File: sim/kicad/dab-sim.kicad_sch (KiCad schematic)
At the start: 25 parts

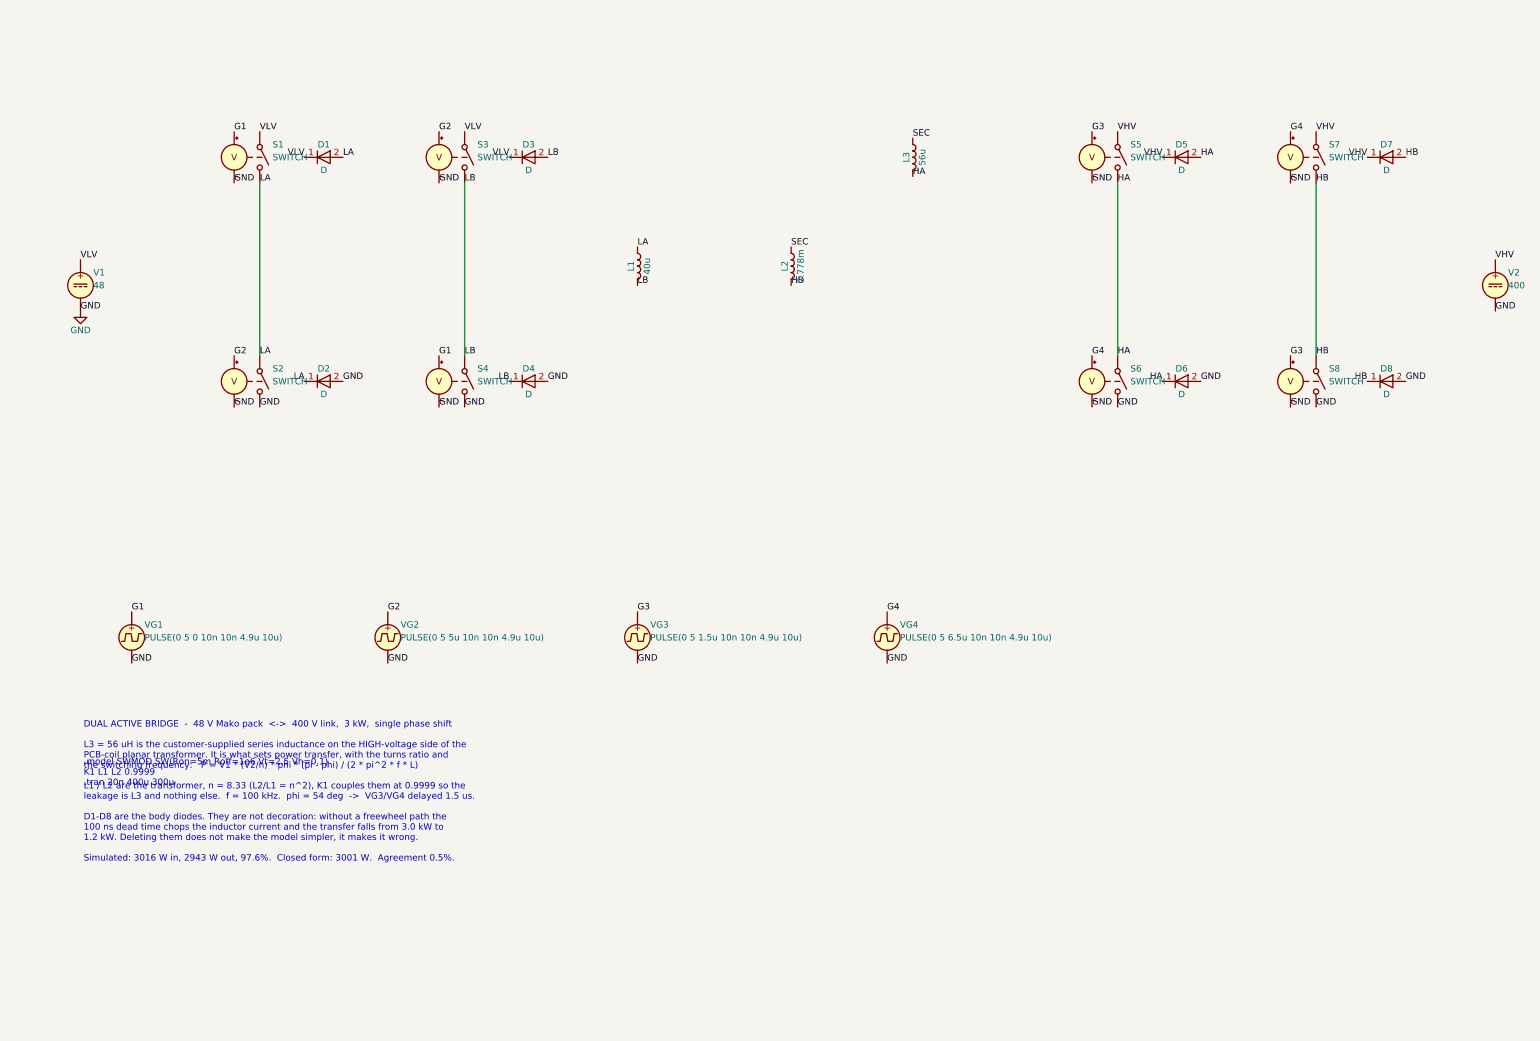
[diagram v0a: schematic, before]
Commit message: Redraw the DAB schematic with wires instead of net labels
A schematic wired only by net names is correct for the netlister and
useless to a human - you cannot trace the bridge by eye. Rebuilt so that
every power connection is a drawn line: both DC rails, the four bridge
legs, the body diodes, the transformer between the low-voltage midpoints
and the 56 uH in the secondary path. Only the four gate nets stay as
labels, which is normal practice; drawing them would put eight wires
across the sheet for nothing. The power nets now carry names as well as
wires, so the exported netlist reads VLV_48V / LA / LB / HA / HB /
VHV_400V rather than Net-_D1-A_.

The rails are drawn above and below the switch rows with stubs down to
each pin, not straight across them: the SWITCH symbol puts its control
pins at the same heights as its power pins, so a rail across a switch row
shorts the supply to the gate net. That is in the README, along with the
Sim.* instance-property trap.

Rebuilt from scratch and independently reproduces the previous result:
3005 W in, 2938 W out, 97.8%, against the closed form's 3001 W - 0.1%.

Co-Authored-By: Claude Opus 5 <noreply@anthropic.com>
Claude-Session: https://claude.ai/code/session_018xNdiSQv3JdagdWVUHe6u6
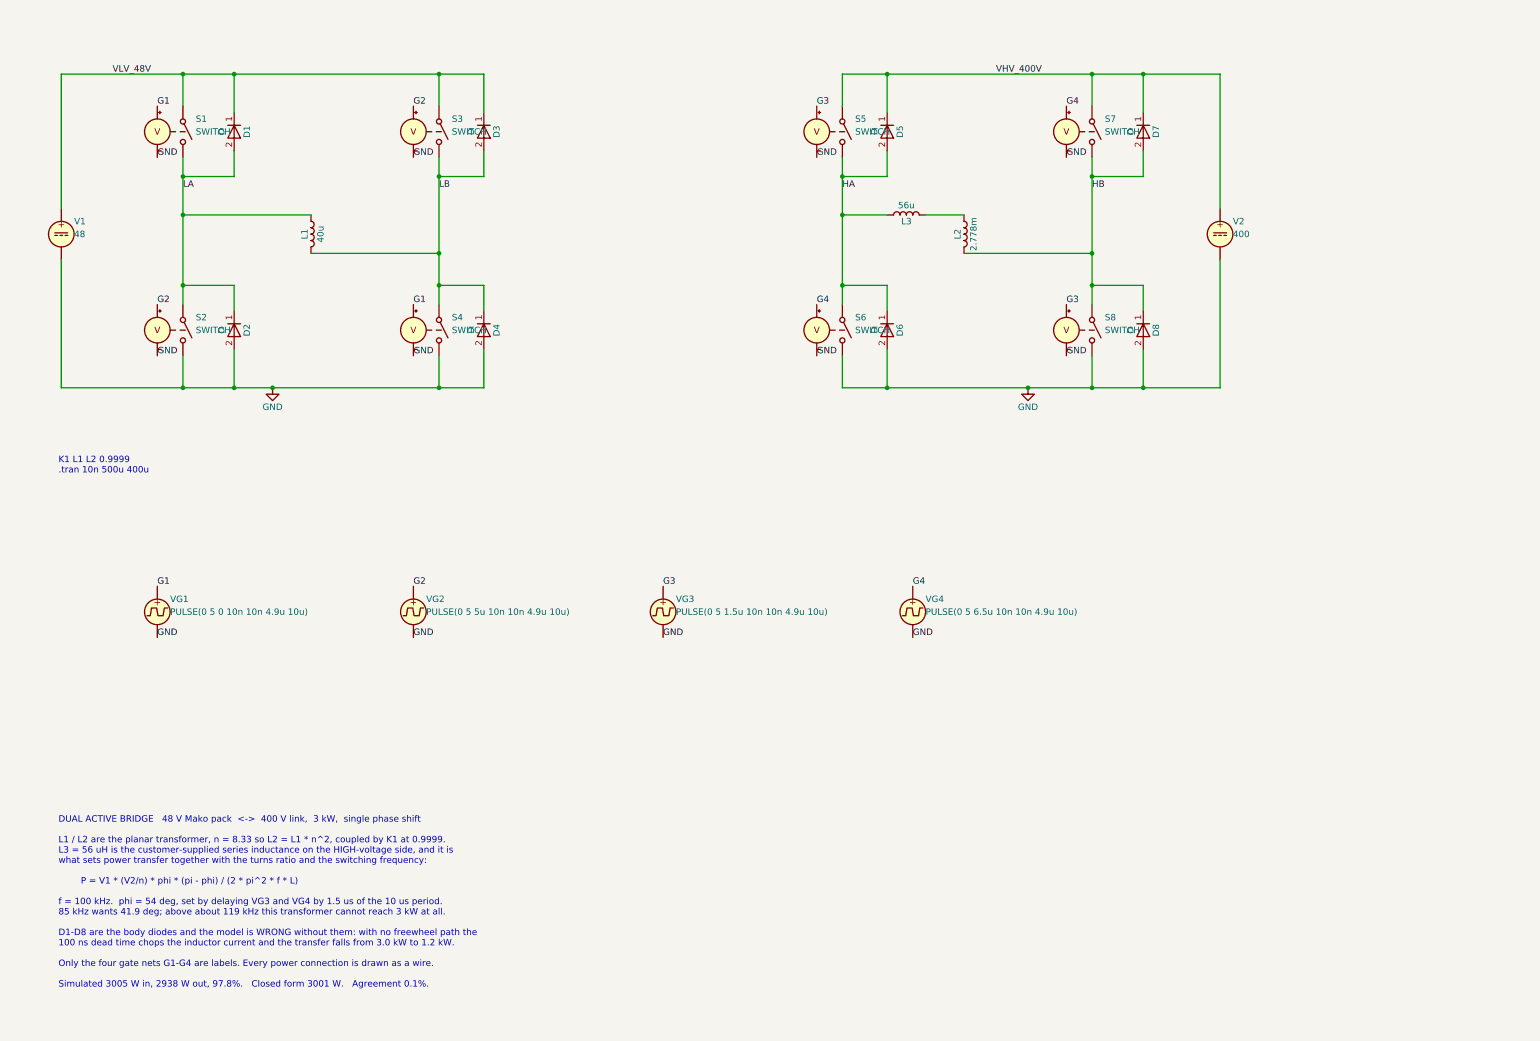
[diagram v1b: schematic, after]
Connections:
- net HA: now also L3.1; no longer L3.2
- net SEC: no longer names the net of L2.1
- net SEC: now also L3.2; no longer L3.1
- net VHV renamed VHV_400V
- net VLV renamed VLV_48V
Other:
- note added: "DUAL ACTIVE BRIDGE 48 V Mako pack <-> 400 V link, 3 kW, single phase shift L1 / L2 are the planar transformer, n = 8.33 so L2 = L1 * n^2, coupled by K1 at 0.9999. L3 = 56 uH is the customer-supplied series inductance on the HIGH-voltage side, and it is what sets power transfer together with the turns ratio and the switching frequency: P = V1 * (V2/n) * phi * (pi - phi) / (2 * pi^2 * f * L) f = 10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"
- note added: "K1 L1 L2 0.9999 .tran 10n 500u 400u"
- note removed: ".model SWMOD SW(Ron=5m Roff=1e6 Vt=2.5 Vh=0.1) K1 L1 L2 0.9999 .tran 20n 400u 300u"
- note removed: "DUAL ACTIVE BRIDGE - 48 V Mako pack <-> 400 V link, 3 kW, single phase shift L3 = 56 uH is the customer-supplied series inductance on the HIGH-voltage side of the PCB-coil planar transformer. It is what sets power transfer, with the turns ratio and the switching frequency: P = V1 * (V2/n) * phi * (pi - phi) / (2 * pi^2 * f * L) L1 / L2 are the transformer, n = 8.33 (L2/L1 = n^2), K1 couples them 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"

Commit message: Replace the K directive with a transformer subcircuit KiCad resolves itself
Three failures in a row all had the same root: mutual coupling reaching
ngspice through schematic text. K is a DEVICE line, not a dot command, and
the GUI netlister prepends a dot to any directive lacking one, so a bare K
arrives as ".k1" and the circuit will not parse. A relative .include fails
too - KiCad drives ngspice as a shared library and hands it the netlist in
memory, leaving no file for a relative path to resolve against.

The windings and their coupling now live in xfmr.lib as a subcircuit,
attached to a real Device:Transformer_1P_1S symbol by Sim.Library =
${KIPRJMOD}/xfmr.lib. Verified that KiCad resolves that variable itself
and emits an absolute, quoted .include: absolute so the shared library
finds it, quoted so a path containing spaces works, and portable because
the variable is resolved at netlist time. Verified separately that
${KIPRJMOD} is NOT expanded in schematic text, which is why the directive
route could never have been made portable.

The sheet also reads better for it: two H-bridges either side of an actual
transformer symbol, with the 56 uH in the secondary, rather than two
disconnected inductors coupled by an invisible statement.

Caught and fixed a short of my own making on the way - the wire routing
pin AA around to the far bridge leg ran straight through pin AB, which the
netlist showed as "XT1 /LA /LA". Also removed four floating wire stubs
left where L1 and L2 had been.

Electrically identical to the verified version, to six figures: 3005.3 W
in, 2938.4 W out, 9.511 A rms, against the closed form's 3001 W.

Co-Authored-By: Claude Opus 5 <noreply@anthropic.com>
Claude-Session: https://claude.ai/code/session_018xNdiSQv3JdagdWVUHe6u6
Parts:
- removed L1: 40u, symbol Device:L
- removed L2: 2.778m, symbol Device:L
- added T1: XFMR 8.33:1, symbol Device:Transformer_1P_1S
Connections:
- net HA: now also L3.2; no longer L3.1
- net HB: now also T1.4 (SB)
- net LA: now also T1.1 (AA)
- net LB: now also T1.2 (AB)
- new net: L3.1, T1.3 (SA)
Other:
- note added: ".tran 10n 500u 400u"
- note added: "DUAL ACTIVE BRIDGE 48 V Mako pack <-> 400 V link, 3 kW, single phase shift T1 is the planar transformer, n = 8.33. Its windings and their mutual coupling live in xfmr.lib, attached to T1 by Sim.Library = ${KIPRJMOD}/xfmr.lib, and KiCad resolves that itself into an absolute .include when it builds the netlist. That indirection is not decoration. K is a DEVICE line in SPICE, not a dot command, and 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"
- note removed: "DUAL ACTIVE BRIDGE 48 V Mako pack <-> 400 V link, 3 kW, single phase shift L1 / L2 are the planar transformer, n = 8.33 so L2 = L1 * n^2, coupled by K1 at 0.9999. L3 = 56 uH is the customer-supplied series inductance on the HIGH-voltage side, and it is what sets power transfer together with the turns ratio and the switching frequency: P = V1 * (V2/n) * phi * (pi - phi) / (2 * pi^2 * f * L) f = 10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"
- note removed: "K1 L1 L2 0.9999 .tran 10n 500u 400u"
- moved on the sheet: L3
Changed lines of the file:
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@@
-	)
-	(junction
-		(at 59.69 96.52)
-		(diameter 0)
-	)
-	(junction
-		(at 110.49 104.14)
-		(diameter 0)
 	)
 	(junction
@@
 	)
 	(junction
-		(at 190.5 96.52)
-		(diameter 0)
-	)
-	(junction
-		(at 240.03 104.14)
-		(diameter 0)
-	)
-	(junction
 		(at 77.47 130.81)
 		(diameter 0)
@@
 		(diameter 0)
 	)
+	(junction
+		(at 110.49 105.41)
+		(diameter 0)
+	)
+	(junction
+		(at 139.7 105.41)
+		(diameter 0)
+	)
+	(junction
+		(at 59.69 100.33)
+		(diameter 0)
+	)
+	(junction
+		(at 190.5 105.41)
+		(diameter 0)
+	)
+	(junction
+		(at 240.03 100.33)
+		(diameter 0)
+	)
 	(wire
 		(pts
@@
 	(wire
 		(pts
-			(xy 59.69 96.52)
-			(xy 85.09 96.52)
-		)
-	)
-	(wire
-		(pts
-			(xy 85.09 104.14)
-			(xy 110.49 104.14)
-		)
-	)
-	(wire
-		(pts
 			(xy 265.43 95.25)
 			(xy 265.43 68.58)
@@
 	(wire
 		(pts
-			(xy 190.5 96.52)
-			(xy 199.39 96.52)
-		)
-	)
-	(wire
-		(pts
-			(xy 207.01 96.52)
-			(xy 214.63 96.52)
-		)
-	)
-	(wire
-		(pts
-			(xy 214.63 104.14)
-			(xy 240.03 104.14)
-		)
-	)
-	(text "K1 L1 L2 0.9999\n.tran 10n 500u 400u"
-		(at 35 148 0)
+			(xy 139.7 105.41)
+			(xy 110.49 105.41)
+		)
+	)
+	(wire
+		(pts
+			(xy 25.4 100.33)
+			(xy 59.69 100.33)
+		)
+	)
+	(wire
+		(pts
+			(xy 160.02 105.41)
+			(xy 171.45 105.41)
+		)
+	)
+	(wire
+		(pts
+			(xy 179.07 105.41)
+			(xy 190.5 105.41)
+		)
+	)
+	(wire
+		(pts
+			(xy 160.02 95.25)
+			(xy 160.02 59.69)
+		)
+	)
+	(wire
+		(pts
+			(xy 160.02 59.69)
+			(xy 275.59 59.69)
+		)
+	)
+	(wire
+		(pts
+			(xy 275.59 59.69)
+			(xy 275.59 100.33)
+		)
+	)
+	(wire
+		(pts
+			(xy 275.59 100.33)
+			(xy 240.03 100.33)
+		)
+	)
+	(wire
+		(pts
+			(xy 139.7 95.25)
+			(xy 139.7 55.88)
+		)
+	)
+	(wire
+		(pts
+			(xy 139.7 55.88)
+			(xy 25.4 55.88)
+		)
+	)
+	(wire
+		(pts
+			(xy 25.4 55.88)
+			(xy 25.4 100.33)
+		)
+	)
+	(text ".tran 10n 500u 400u"
+		(at 35 160 0)
 		(effects
 			(font
@@
 		)
 	)
-  (text "DUAL ACTIVE BRIDGE   48 V Mako pack  <->  400 V link,  3 kW,  single phase shift\n\nL1 / L2 are the planar transformer, n = 8.33 so L2 = L1 * n^2, coupled by K1 at 0.9999.\nL3 = 56 uH is the customer-supplied series inductance on the HIGH-voltage side, and it is\nwhat sets power transfer together with the turns ratio and the switching frequency:\n\n        P = V1 * (V2/n) * phi * (pi - phi) / (2 * pi^2 * f * L)\n\nf = 100 kHz.  phi = 54 deg, set by delaying VG3 and VG4 by 1.5 us of the 10 us period.\n85 kHz wants 41.9 deg; above about 119 kHz this transformer cannot reach 3 kW at all.\n\nD1-D8 are the body diodes and the model is WRONG without them: with no freewheel path the\n100 ns dead time chops the inductor current and the transfer falls from 3.0 kW to 1.2 kW.\n\nOnly the four gate nets G1-G4 are labels. Every power connection is drawn as a wire.\n\nSimulated 3005 W in, 2938 W out, 97.8%.   Closed form 3001 W.   Agreement 0.1%."
-    (at 35 250 0)
+  (text "DUAL ACTIVE BRIDGE   48 V Mako pack  <->  400 V link,  3 kW,  single phase shift\n\nT1 is the planar transformer, n = 8.33. Its windings and their mutual coupling live in\nxfmr.lib, attached to T1 by Sim.Library = ${KIPRJMOD}/xfmr.lib, and KiCad resolves that\nitself into an absolute .include when it builds the netlist.\n\nThat indirection is not decoration. K is a DEVICE line in SPICE, not a dot command, and\nthe GUI simulator prepends a dot to any schematic text directive that lacks one - so a\nbare \"K1 L1 L2 0.9999\" on the sheet reaches ngspice as \".k1 ...\" and the circuit will not\nparse. A relative \".include\" does not work either, because KiCad drives ngspice as a\nshared library and hands it the netlist in memory, with no file for a relative path to\nresolve against. Sim.Library avoids both: KiCad does the resolving.\n\nL3 = 56 uH is the customer-supplied series inductance on the HIGH-voltage side, and with\nthe turns ratio and the frequency it is what sets power transfer:\n\n        P = V1 * (V2/n) * phi * (pi - phi) / (2 * pi^2 * f * L)\n\nf = 100 kHz.  phi = 54 deg, set by delaying VG3 and VG4 by 1.5 us of the 10 us period.\n85 kHz wants 41.9 deg; above about 119 kHz this transformer cannot reach 3 kW at all.\n\nD1-D8 are the body diodes and the model is WRONG without them: with no freewheel path the\n100 ns dead time chops the inductor current and the transfer falls from 3.0 kW to 1.2 kW.\n\nOnly the four gate nets G1-G4 are labels. Every power connection is drawn as a wire.\n\nSimulated 3005 W in, 2938 W out, 97.8%.   Closed form 3001 W.   Agreement 0.1%."
+    (at 35 255 0)
     (effects (font (size 1.27 1.27)) (justify left bottom))
   )
@@
 	(symbol
 		(lib_id "Device:L")
-		(at 85.09 100.33 0)
-		(unit 1)
-		(in_bom yes)
-		(on_board yes)
-		(dnp no)
-		(property "Reference" "L1"
-			(at 83.82 100.33 90)
-			(effects
-				(font
-					(size 1.27 1.27)
-				)
-			)
-		)
-		(property "Value" "40u"
-			(at 86.995 100.33 90)
-			(effects
-				(font
-					(size 1.27 1.27)
-				)
-			)
-		)
-		(property "Footprint" ""
-			(at 85.09 100.33 0)
-			(hide yes)
-			(effects
-				(font
-					(size 1.27 1.27)
-				)
-			)
-		)
-		(property "Datasheet" ""
-			(at 85.09 100.33 0)
-			(hide yes)
-			(effects
-				(font
-					(size 1.27 1.27)
-				)
-			)
-		)
-		(instances
-			(project "dab-sim"
-				(path "8bdc63a0-d120-4e49-a0a7-406cc55b9f90"
-					(reference "L1")
-					(unit 1)
-				)
-			)
-		)
-	)
-	(symbol
-		(lib_id "Device:L")
-		(at 214.63 100.33 0)
-		(unit 1)
-		(in_bom yes)
-		(on_board yes)
-		(dnp no)
-		(property "Reference" "L2"
-			(at 213.36 100.33 90)
-			(effects
-				(font
-					(size 1.27 1.27)
-				)
-			)
-		)
-		(property "Value" "2.778m"
-			(at 216.535 100.33 90)
-			(effects
-				(font
-					(size 1.27 1.27)
-				)
-			)
-		)
-		(property "Footprint" ""
-			(at 214.63 100.33 0)
-			(hide yes)
-			(effects
-				(font
-					(size 1.27 1.27)
-				)
-			)
-		)
-		(property "Datasheet" ""
-			(at 214.63 100.33 0)
-			(hide yes)
-			(effects
-				(font
-					(size 1.27 1.27)
-				)
-			)
-		)
-		(instances
-			(project "dab-sim"
-				(path "8bdc63a0-d120-4e49-a0a7-406cc55b9f90"
-					(reference "L2")
-					(unit 1)
-				)
-			)
-		)
-	)
-	(symbol
-		(lib_id "Device:L")
-		(at 203.2 96.52 90)
+		(at 175.26 105.41 90)
 		(unit 1)
 		(in_bom yes)
@@
 		(dnp no)
 		(property "Reference" "L3"
-			(at 203.2 97.79 90)
+			(at 175.26 106.68 90)
 			(effects
 				(font
@@
 		)
 		(property "Value" "56u"
-			(at 203.2 94.615 90)
-			(effects
-				(font
-					(size 1.27 1.27)
-				)
-			)
-		)
-		(property "Footprint" ""
-			(at 203.2 96.52 0)
-			(hide yes)
-			(effects
-				(font
-					(size 1.27 1.27)
-				)
-			)
-		)
-		(property "Datasheet" ""
-			(at 203.2 96.52 0)
+			(at 175.26 103.505 90)
+			(effects
+				(font
+					(size 1.27 1.27)
+				)
+			)
+		)
+		(property "Footprint" ""
+			(at 175.26 105.41 0)
+			(hide yes)
+			(effects
+				(font
+					(size 1.27 1.27)
+				)
+			)
+		)
+		(property "Datasheet" ""
+			(at 175.26 105.41 0)
 			(hide yes)
 			(effects
@@
 					(unit 1)
 				)
+			)
+		)
+	)
+	(symbol
+		(lib_id "Device:Transformer_1P_1S")
+		(at 149.86 100.33 0)
+		(unit 1)
+		(in_bom yes)
+		(on_board yes)
+		(dnp no)
+		(property "Reference" "T1"
+			(at 149.86 93.98 0)
+			(effects
+				(font
+					(size 1.27 1.27)
+				)
+			)
+		)
+		(property "Value" "XFMR 8.33:1"
+			(at 149.86 107.95 0)
+			(effects
+				(font
+					(size 1.27 1.27)
+				)
+			)
+		)
+		(property "Footprint" ""
+			(at 149.86 100.33 0)
+			(hide yes)
+			(effects
+				(font
+					(size 1.27 1.27)
+				)
+			)
+		)
+		(property "Datasheet" ""
+			(at 149.86 100.33 0)
+			(hide yes)
+			(effects
+				(font
+					(size 1.27 1.27)
+				)
+			)
+		)
+		(property "Sim.Device" "SUBCKT"
+			(at 149.86 100.33 0)
+			(hide yes)
+			(effects
+				(font
+					(size 1.27 1.27)
+				)
+			)
+		)
+		(property "Sim.Name" "XFMR"
+			(at 149.86 100.33 0)
+			(hide yes)
+			(effects
+				(font
+					(size 1.27 1.27)
+				)
+			)
+		)
+		(property "Sim.Library" "${KIPRJMOD}/xfmr.lib"
+			(at 149.86 100.33 0)
+			(hide yes)
+			(effects
+				(font
+					(size 1.27 1.27)
+				)
+			)
+		)
+		(property "Sim.Pins" "1=1 2=2 3=3 4=4"
+			(at 149.86 100.33 0)
+			(hide yes)
+			(effects
+				(font
+					(size 1.27 1.27)
+				)
+			)
+		)
+		(instances
+			(project "dab-sim"
+				(path "8bdc63a0-d120-4e49-a0a7-406cc55b9f90"
+					(reference "T1")
+					(unit 1)
+				)
